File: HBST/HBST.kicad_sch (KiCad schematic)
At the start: 14 parts, among them J1 Conn_01x06_Pin, J3 Conn_01x04_Pin, J4 Conn_01x13_Pin, J5 Conn_01x09_Pin

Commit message: updated design
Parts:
- added R3, R4: 50, Resistor_SMD:R_0805_2012Metric_Pad1.20x1.40mm_HandSolder, symbol Device:R
- added TP3, TP4: TestPoint_Small, TestPoint:TestPoint_Pad_D1.0mm, symbol Connector:TestPoint_Small
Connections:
- net GND: now also R3.2, R4.2
- new net: R3.1, TP3.1
- new net: R4.1, TP4.1
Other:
- moved on the sheet: J1, J4, J5, JP2, R1, R2, TP1, TP2, U1A, U1B, U1C, U1E

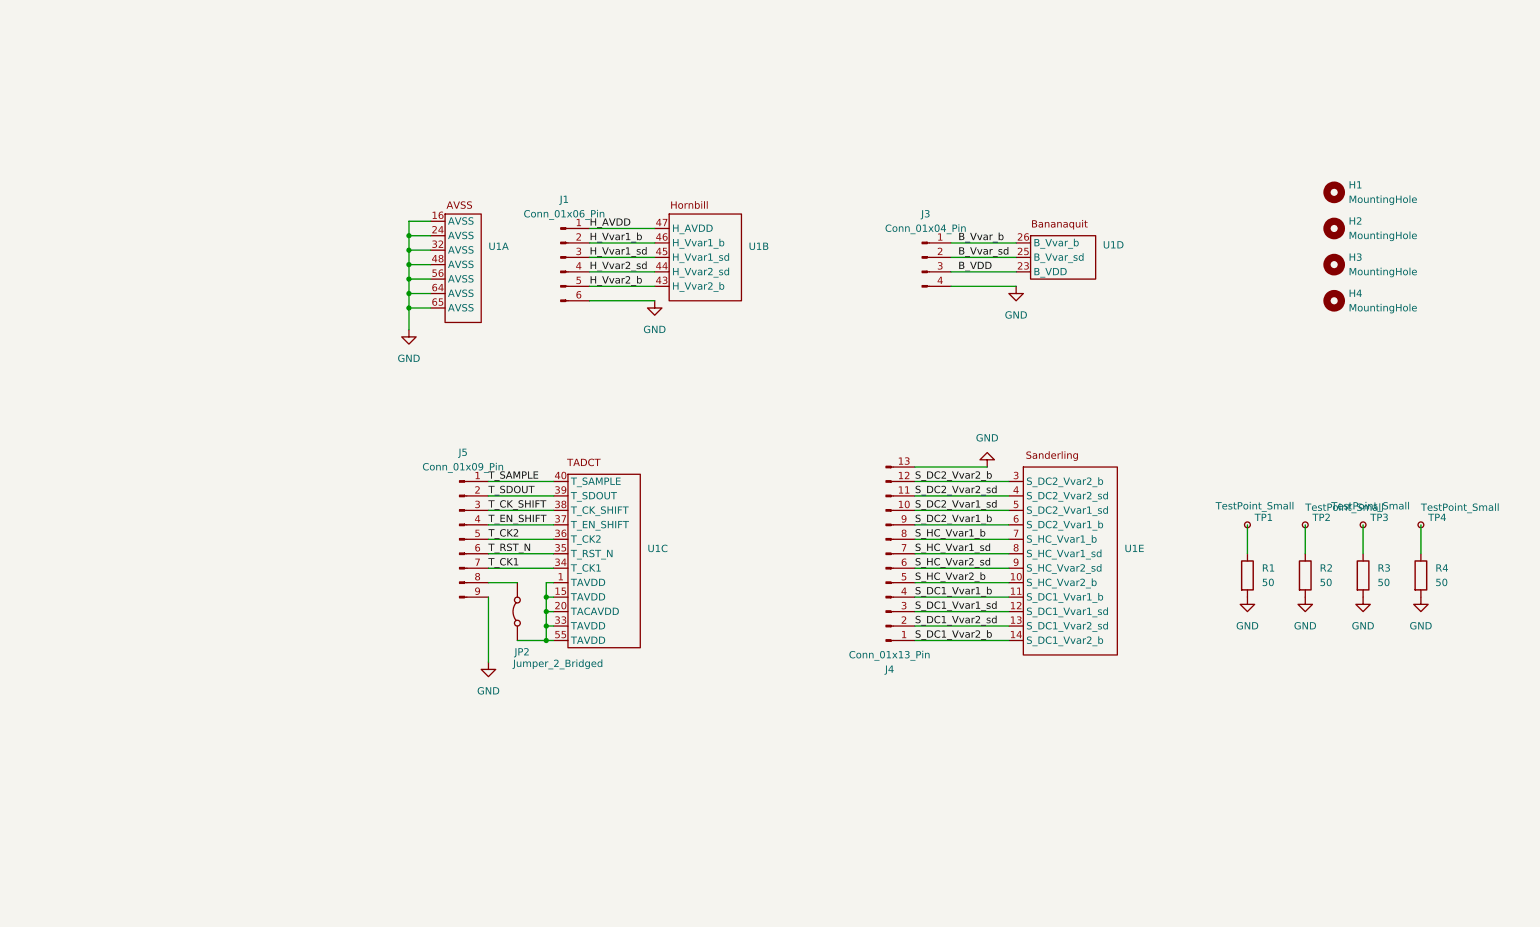
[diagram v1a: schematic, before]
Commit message: added decoupling capacitors and fixed copper fill zone on In2 copper layer
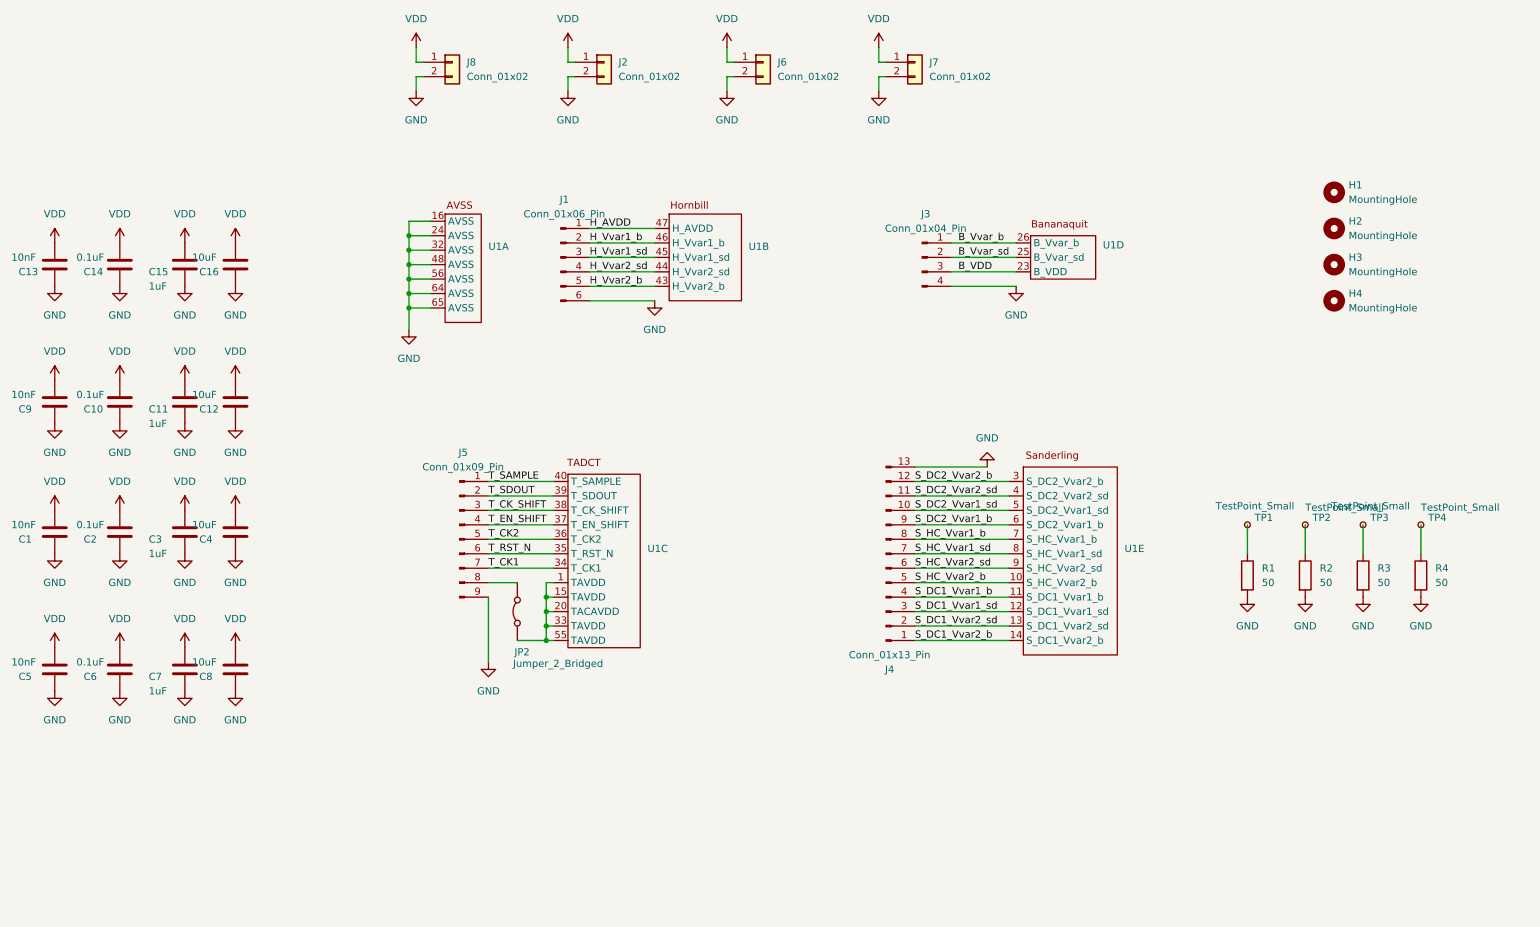
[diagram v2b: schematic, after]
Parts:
- added C1, C13, C5, C9: 10nF, Capacitor_SMD:C_0805_2012Metric, symbol Device:C
- added C10, C14, C2, C6: 0.1uF, Capacitor_SMD:C_0805_2012Metric, symbol Device:C
- added C11, C15, C3, C7: 1uF, Capacitor_SMD:C_0805_2012Metric, symbol Device:C
- added C12, C16, C4, C8: 10uF, Capacitor_SMD:C_0805_2012Metric, symbol Device:C
- added J2, J6, J7, J8: Conn_01x02, Connector_PinHeader_2.54mm:PinHeader_1x02_P2.54mm_Horizontal, symbol Connector_Generic:Conn_01x02
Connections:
- net GND: now also C1.1, C10.1, C11.1, C12.1, C13.1, C14.1, C15.1, C16.1, C2.1, C3.1, C4.1, C5.1, C6.1, C7.1, C8.1, C9.1, J2.2 (Pin_2), J6.2 (Pin_2), J7.2 (Pin_2), J8.2 (Pin_2)
- new net VDD: C1.2, C10.2, C11.2, C12.2, C13.2, C14.2, C15.2, C16.2, C2.2, C3.2, C4.2, C5.2, C6.2, C7.2, C8.2, C9.2, J2.1 (Pin_1), J6.1 (Pin_1), J7.1 (Pin_1), J8.1 (Pin_1)

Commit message: minor update
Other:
- moved on the sheet: C1, C10, C11, C12, C13, C14, C15, C16, C2, C3, C4, C5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

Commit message: fixed to correct package and minor component placement changes
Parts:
- U1: footprint Package_DFN_QFN:QFN-64-1EP_8x8mm_P0.4mm_EP6.5x6.5mm_ThermalVias -> Package_DFN_QFN:QFN-64-1EP_9x9mm_P0.5mm_EP6x6mm
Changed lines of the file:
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@@
 (kicad_sch
-	(version 20231120)
+	(version 20241209)
 	(generator "eeschema")
-	(generator_version "8.0")
+	(generator_version "9.0")
 	(paper "A4")
 	(junction
@@
 	(label "S_DC2_Vvar2_b"
 		(at 177.8 97.79 0)
-		(fields_autoplaced yes)
 		(effects
 			(font
@@
 	(label "T_CK1"
 		(at 102.87 113.03 0)
-		(fields_autoplaced yes)
 		(effects
 			(font
@@
 	(label "T_CK_SHIFT"
 		(at 102.87 102.87 0)
-		(fields_autoplaced yes)
 		(effects
 			(font
@@
 	(label "B_VDD"
 		(at 185.42 60.96 0)
-		(fields_autoplaced yes)
 		(effects
 			(font
@@
 	(label "T_CK2"
 		(at 102.87 107.95 0)
-		(fields_autoplaced yes)
 		(effects
 			(font
@@
 	(label "H_Vvar2_sd"
 		(at 120.65 60.96 0)
-		(fields_autoplaced yes)
 		(effects
 			(font
@@
 	(label "H_AVDD"
 		(at 120.65 53.34 0)
-		(fields_autoplaced yes)
 		(effects
 			(font
@@
 	(label "S_HC_Vvar1_b"
 		(at 177.8 107.95 0)
-		(fields_autoplaced yes)
 		(effects
 			(font
@@
 	(label "S_DC1_Vvar2_b"
 		(at 177.8 125.73 0)
-		(fields_autoplaced yes)
 		(effects
 			(font
@@
 	(label "T_RST_N"
 		(at 102.87 110.49 0)
-		(fields_autoplaced yes)
 		(effects
 			(font
@@
 	(label "S_HC_Vvar2_sd"
 		(at 177.8 113.03 0)
-		(fields_autoplaced yes)
 		(effects
 			(font
@@
 	(label "S_DC2_Vvar1_sd"
 		(at 177.8 102.87 0)
-		(fields_autoplaced yes)
 		(effects
 			(font
@@
 	(label "S_HC_Vvar2_b"
 		(at 177.8 115.57 0)
-		(fields_autoplaced yes)
 		(effects
 			(font
@@
 	(label "T_SDOUT"
 		(at 102.87 100.33 0)
-		(fields_autoplaced yes)
 		(effects
 			(font
@@
 	(label "H_Vvar2_b"
 		(at 120.65 63.5 0)
-		(fields_autoplaced yes)
 		(effects
 			(font
@@
 	(label "B_Vvar_sd"
 		(at 185.42 58.42 0)
-		(fields_autoplaced yes)
 		(effects
 			(font
@@
 	(label "T_EN_SHIFT"
 		(at 102.87 105.41 0)
-		(fields_autoplaced yes)
 		(effects
 			(font
@@
 	(label "H_Vvar1_b"
 		(at 120.65 55.88 0)
-		(fields_autoplaced yes)
 		(effects
 			(font
@@
 	(label "T_SAMPLE"
 		(at 102.87 97.79 0)
-		(fields_autoplaced yes)
 		(effects
 			(font
@@
 	(label "S_DC1_Vvar1_sd"
 		(at 177.8 120.65 0)
-		(fields_autoplaced yes)
 		(effects
 			(font
@@
 	(label "S_DC2_Vvar2_sd"
 		(at 177.8 100.33 0)
-		(fields_autoplaced yes)
 		(effects
 			(font
@@
 	(label "S_HC_Vvar1_sd"
 		(at 177.8 110.49 0)
-		(fields_autoplaced yes)
 		(effects
 			(font
@@
 	(label "B_Vvar_b"
 		(at 185.42 55.88 0)
-		(fields_autoplaced yes)
 		(effects
 			(font
@@
 	(label "S_DC1_Vvar2_sd"
 		(at 177.8 123.19 0)
-		(fields_autoplaced yes)
 		(effects
 			(font
@@
 	(label "S_DC2_Vvar1_b"
 		(at 177.8 105.41 0)
-		(fields_autoplaced yes)
 		(effects
 			(font
@@
 	(label "H_Vvar1_sd"
 		(at 120.65 58.42 0)
-		(fields_autoplaced yes)
 		(effects
 			(font
@@
 	(label "S_DC1_Vvar1_b"
 		(at 177.8 118.11 0)
-		(fields_autoplaced yes)
 		(effects
 			(font
@@
 			)
 		)
-		(property "Footprint" "Package_DFN_QFN:QFN-64-1EP_8x8mm_P0.4mm_EP6.5x6.5mm_ThermalVias"
+		(property "Footprint" "Package_DFN_QFN:QFN-64-1EP_9x9mm_P0.5mm_EP6x6mm"
 			(at 83.82 77.47 0)
 			(effects
@@
 			)
 		)
-		(property "Footprint" "Package_DFN_QFN:QFN-64-1EP_8x8mm_P0.4mm_EP6.5x6.5mm_ThermalVias"
+		(property "Footprint" "Package_DFN_QFN:QFN-64-1EP_9x9mm_P0.5mm_EP6x6mm"
 			(at 189.23 80.01 0)
 			(effects
@@
 			)
 		)
-		(property "Footprint" "Package_DFN_QFN:QFN-64-1EP_8x8mm_P0.4mm_EP6.5x6.5mm_ThermalVias"
+		(property "Footprint" "Package_DFN_QFN:QFN-64-1EP_9x9mm_P0.5mm_EP6x6mm"
 			(at 125.73 81.28 0)
 			(effects
@@
 			)
 		)
-		(property "Footprint" "Package_DFN_QFN:QFN-64-1EP_8x8mm_P0.4mm_EP6.5x6.5mm_ThermalVias"
+		(property "Footprint" "Package_DFN_QFN:QFN-64-1EP_9x9mm_P0.5mm_EP6x6mm"
 			(at 107.95 128.27 0)
 			(effects
@@
 			)
 		)
-		(property "Footprint" "Package_DFN_QFN:QFN-64-1EP_8x8mm_P0.4mm_EP6.5x6.5mm_ThermalVias"
+		(property "Footprint" "Package_DFN_QFN:QFN-64-1EP_9x9mm_P0.5mm_EP6x6mm"
 			(at 189.23 134.62 0)
 			(effects
@@
 		)
 	)
+	(embedded_fonts no)
 )
